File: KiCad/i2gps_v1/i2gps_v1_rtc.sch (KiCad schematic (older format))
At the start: 7 parts, among them U4 DS3231N

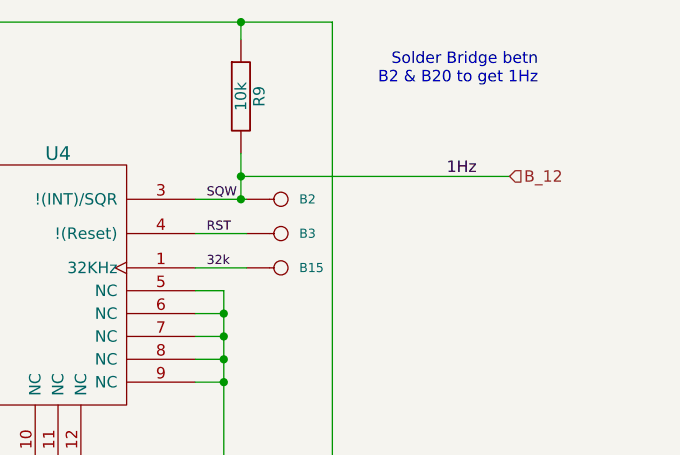
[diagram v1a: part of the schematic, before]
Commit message: i2gps_v1 : this project is merged with i2sd_v3. GPS header to be added
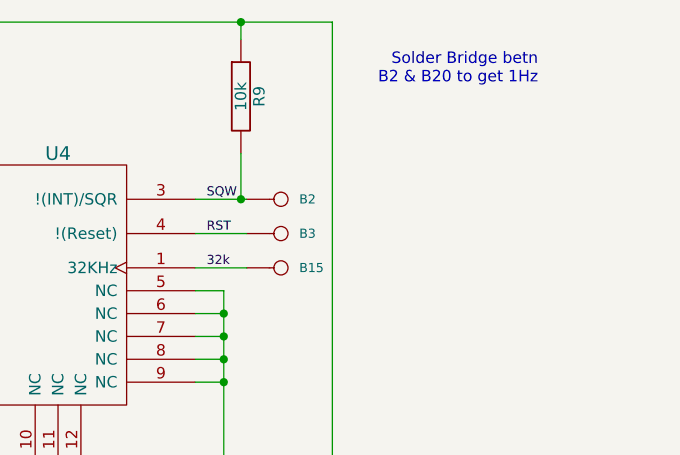
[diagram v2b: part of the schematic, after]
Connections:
- net labels removed: 1Hz, B_12
- wire segments 42 -> 41
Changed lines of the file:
@@
-EESchema Schematic File Version 2  date 2/23/2012 5:46:03 PM
+EESchema Schematic File Version 2  date 3/9/2012 6:29:22 PM
 LIBS:i2gps_v1
 LIBS:power
@@
 Sheet 2 2
 Title "Buckler, i2sd, v3, with RTC, with HW addressing"
-Date "23 feb 2012"
+Date "9 mar 2012"
 Rev "3"
 Comp "WyoLum"
@@
 Wire Wire Line
 	7250 4650 6950 4650
-Wire Wire Line
-	6650 2350 7825 2350
-Connection ~ 6650 2350
 Text Label 6950 4800 0    60   ~ 0
 RST
@@
 Text Notes 7950 1950 2    50   ~ 0
 Solder Bridge betn\nB2 & B20 to get 1Hz
-Text HLabel 7825 2350 2    50   Input ~ 0
-B_12
-Text Label 7550 2350 0    50   ~ 0
-1Hz
 $Comp
 L R R9

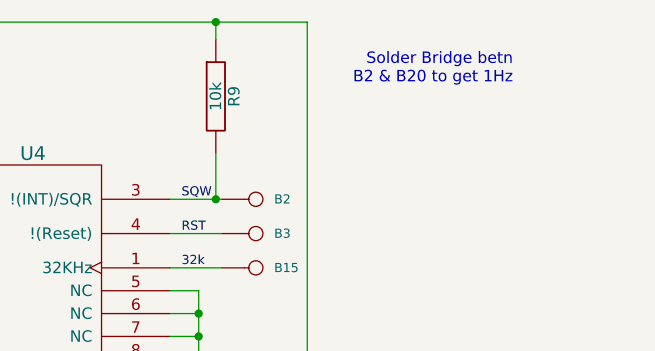
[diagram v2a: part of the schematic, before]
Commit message: 
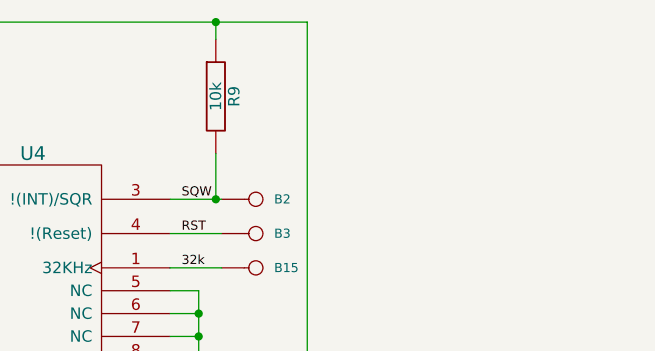
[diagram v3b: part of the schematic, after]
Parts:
- BT1: footprint CR2032 -> CR1632
- C9: footprint C2 -> c_0805
- R9: footprint rc03_vert_LED -> r_0805
- U4: footprint DIP-24__600_ELL -> DS3231
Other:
- note removed: "Solder Bridge betn\nB2 & B20 to get 1Hz"
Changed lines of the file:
@@
-EESchema Schematic File Version 2  date 3/9/2012 6:29:22 PM
+EESchema Schematic File Version 2  date 3/10/2012 5:22:51 PM
 LIBS:i2gps_v1
 LIBS:power
@@
 Sheet 2 2
 Title "Buckler, i2sd, v3, with RTC, with HW addressing"
-Date "9 mar 2012"
+Date "10 mar 2012"
 Rev "3"
 Comp "WyoLum"
@@
 Text HLabel 7250 4350 2    60   Input ~ 0
 BAT
-Text Notes 7950 1950 2    50   ~ 0
-Solder Bridge betn\nB2 & B20 to get 1Hz
 $Comp
 L R R9
@@
 F 0 "R9" V 6730 2000 50  0000 C CNN
 F 1 "10k" V 6650 2000 50  0000 C CNN
-F 2 "rc03_vert_LED" H 6650 2000 60  0001 C CNN
+F 2 "r_0805" H 6650 2000 60  0001 C CNN
 	1    6650 2000
 	1    0    0    -1
@@
 F 0 "U4" H 5850 3350 60  0000 C CNN
 F 1 "DS3231N" H 5250 2400 60  0000 C CNN
-F 2 "DIP-24__600_ELL" H 5550 2800 60  0001 C CNN
+F 2 "DS3231" H 5550 2800 60  0001 C CNN
 	1    5550 2800
 	1    0    0    -1
@@
 F 0 "C9" V 4225 2875 50  0000 L CNN
 F 1 "100n" V 4225 2575 50  0000 L CNN
-F 2 "C2" H 4175 2775 60  0001 C CNN
+F 2 "c_0805" H 4175 2775 60  0001 C CNN
 	1    4175 2775
 	1    0    0    -1
@@
 F 0 "BT1" H 3650 2600 50  0000 C CNN
 F 1 "BATT_RTC" H 3950 2610 50  0000 C CNN
-F 2 "CR2032" H 3950 2800 60  0001 C CNN
+F 2 "CR1632" H 3950 2800 60  0001 C CNN
 F 4 "BU2032SM-HD-GCT-ND " H 3950 2800 60  0001 C CNN "Digikey"
 	1    3950 2800
